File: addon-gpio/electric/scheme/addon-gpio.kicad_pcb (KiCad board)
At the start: 2 copper layers, 85 x 56 mm, 69 parts, among them K1 swd, K10 CONN_3, K11 CONN_3, K12 CONN_3, K13 CONN_3, K14 CONN_3, K15 CONN_3, K16 CONN_3, K17 CONN_3, K18 CONN_3, K19 CONN_3, K2 CONN_3, K20 CONN_3, K21 CONN_3, K22 CONN_3, K23 CONN_3, K24 CONN_3, K25 CONN_3, K26 CONN_3, K27 CONN_3, K28 CONN_3, K29 CONN_3, K3 CONN_3, K30 CONN_3, K31 CONN_3, K32 CONN_3, K4 CONN_3, K5 CONN_3, K6 CONN_3, K7 CONN_3, K8 CONN_3, K9 CONN_3, P1 TST, P2 cross board conn, P3 cross board conn, P4 TST, P5 boot-sel, P6 pwr-ext, P7 rst-2, P8 rst-1, Q1 bc847, Q2 sot223, Q3 IRLML2244, Q4 sot223, Q5 IRLML2244, X1 8MHz

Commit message: Placing components...
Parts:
- C11, C9, Q1, Q2, Q3, Q4, Q5, R10, R6, R7, R8, R9: moved to F.Cu
- moved K5 52.3 mm to (213.6, 129.0), turned to 90 degrees
- moved K6 50.5 mm to (211.1, 129.0), turned to 90 degrees
- moved K7 49.2 mm to (208.5, 129.0), turned to 90 degrees
- moved K11 49.0 mm to (198.4, 129.0), turned to 90 degrees
- moved K8 48.3 mm to (206.0, 129.0), turned to 90 degrees
- moved K10 48.2 mm to (200.9, 129.0), turned to 90 degrees
- moved K9 48.0 mm to (203.5, 129.0), turned to 90 degrees
- moved R6 27.4 mm to (216.7, 179.4)
- moved R7 23.8 mm to (216.7, 177.6)
- moved Q1 18.7 mm to (216.7, 175.0)
- moved C12 18.5 mm to (217.3, 156.6)
- moved C10 16.9 mm to (222.6, 174.1), turned to 270 degrees
- moved C9 14.9 mm to (220.4, 173.1), turned to 270 degrees
- moved K13 13.5 mm to (173.0, 129.0)
- moved K17 13.5 mm to (162.8, 129.0)
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
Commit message: Routing...
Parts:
- added K33: CONN_3, PIN_ARRAY_3X1, F.Cu at (190.8, 129.0)
- moved R3 32.3 mm to (189.6, 135.2), turned to 90 degrees
- moved K19 25.4 mm to (216.2, 129.0)
- moved P5 22.4 mm to (161.6, 148.2)
- moved R2 22.4 mm to (161.6, 145.9)
- moved K30 10.2 mm to (160.3, 129.0)
- moved K31 10.2 mm to (157.7, 129.0)
- moved K32 10.2 mm to (155.2, 129.0)
- moved K20 7.62 mm to (152.7, 129.0)
- moved K21 7.62 mm to (150.1, 129.0)
- moved K29 7.62 mm to (145.0, 129.0)
- moved K22 7.62 mm to (147.6, 129.0)
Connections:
- K10 pad 1: /pin_5 -> /pin_6
- K11 pad 1: /pin_6 -> /pin_7
- K12 pad 1: /pin_7 -> /pin_13
- K18 pad 1: /pin_13 -> /pin_14
- K19 pad 1: /pin_14 -> /pin_0
- K5 pad 1: /pin_0 -> /pin_1
- K6 pad 1: /pin_1 -> /pin_2
- K7 pad 1: /pin_2 -> /pin_3
- K8 pad 1: /pin_3 -> /pin_4
- K9 pad 1: /pin_4 -> /pin_5
- R3 pad 1: /pin_25 -> /pin_28
- stm1 pad 2: /pwr-en -> /pin_24
- stm1 pad 20: /pin_25 -> /pin_28
- stm1 pad 4: /pin_24 -> /pwr-en
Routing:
- net /pin_24: track 0.00 -> 59.1 mm
- net /pin_0: track 0.00 -> 48.0 mm
- net /pin_17: track 0.00 -> 47.4 mm
- net /pin_1: track 0.00 -> 45.4 mm
- net /pin_16: track 0.00 -> 44.5 mm
- net /pin_2: track 0.00 -> 42.8 mm
- net /pin_3: track 0.00 -> 36.0 mm
- net /pin_15: track 0.00 -> 35.9 mm
- net /pin_4: track 0.00 -> 33.9 mm
- net /pin_27: track 0.00 -> 33.8 mm
- net /pin_5: track 0.00 -> 32.2 mm
- net /pin_26: track 0.00 -> 30.9 mm
- net /pin_6: track 0.00 -> 30.5 mm
- net /pin_12: track 0.00 -> 29.7 mm
- net /pin_25: track 0.00 -> 28.8 mm
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
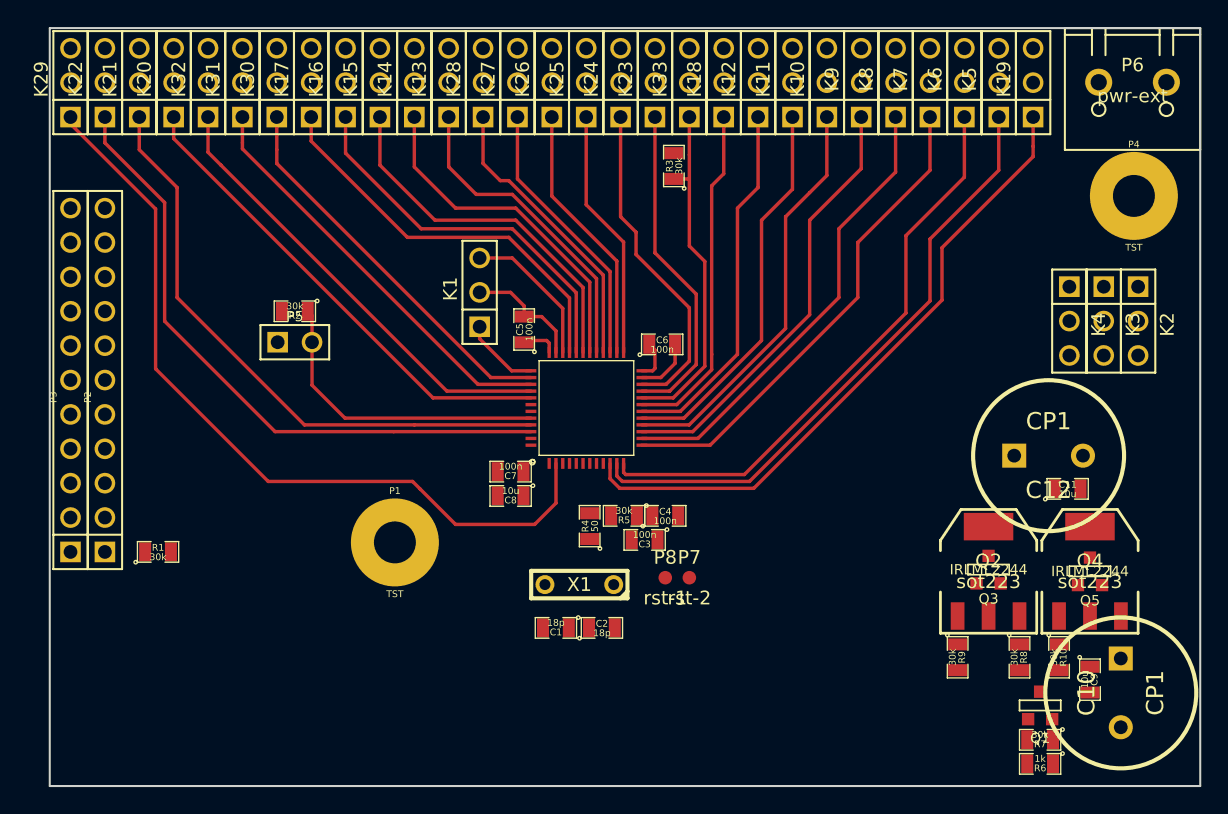
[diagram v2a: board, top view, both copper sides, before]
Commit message: Routed. Making silcography.
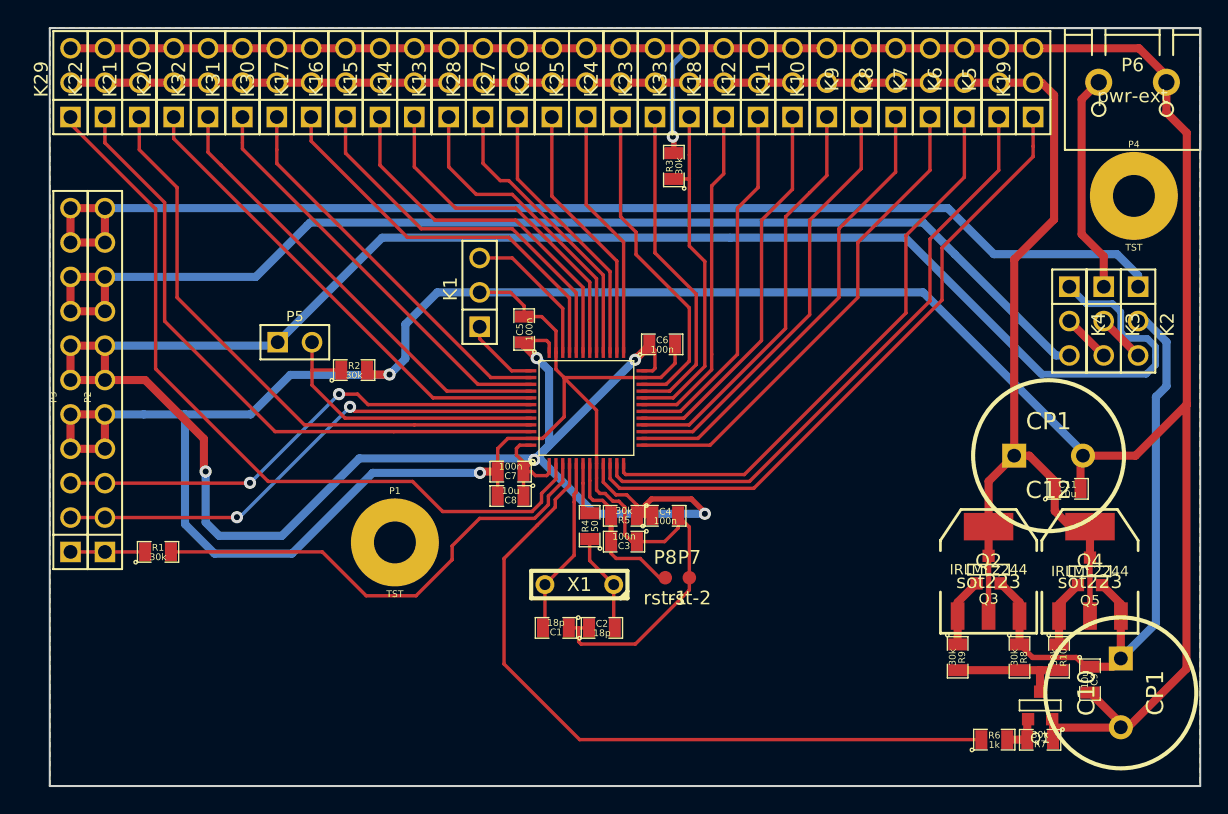
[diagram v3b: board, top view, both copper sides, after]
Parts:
- moved R2 6.17 mm to (166.0, 150.3), turned to 0 degrees
- moved R6 3.83 mm to (213.3, 177.6), turned to 0 degrees
- moved C3 1.53 mm to (185.9, 162.9)
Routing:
- net GND: track 13.2 -> 363.2 mm, vias 0 -> 3
- net VDD: track 5.68 -> 211.6 mm, vias 0 -> 5
- net /pwr-servo: track 0.00 -> 129.2 mm
- net /batt+: track 0.00 -> 89.4 mm
- net /+5v: track 0.00 -> 87.1 mm
- net /pwr-en: track 0.00 -> 54.4 mm
- net N-0000020: track 0.00 -> 47.0 mm
- net /sda-int: track 0.00 -> 37.5 mm, vias 0 -> 2
- net /scl-int: track 0.38 -> 37.1 mm, vias 0 -> 2
- net /wakeup: track 0.00 -> 36.1 mm
- net /pwr-ext: track 0.00 -> 16.3 mm
- net N-0000018: track 0.00 -> 13.2 mm
- net N-0000011: track 0.00 -> 12.5 mm
- net N-0000019: track 0.00 -> 9.08 mm
- net N-0000017: track 0.00 -> 7.34 mm
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- added copper zone on B.Cu, net GND
- added copper zone on F.Cu, net GND
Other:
- board text added: "3.3"
- board text added: "batt"
- board text added: "ext"

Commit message: Made drawing with connections scheme.
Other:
- board text added: "5v"
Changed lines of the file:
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@@
     (area 127.606667 112.000001 242.964763 190.8)
     (thickness 1.6)
-    (drawings 53)
+    (drawings 69)
     (tracks 551)
     (zones 0)
@@
   )
   (setup
-    (last_trace_width 0.4)
+    (last_trace_width 0.254)
     (user_trace_width 0.4)
     (user_trace_width 0.5)
@@
     )
   )
+  (gr_line (start 211 154) (end 211 151) (angle 90) (layer Eco1.User) (width 0.2))
+  (gr_line (start 214.5 154) (end 214.5 151) (angle 90) (layer Eco1.User) (width 0.2))
+  (gr_line (start 213 152.5) (end 214.5 154) (angle 90) (layer Eco1.User) (width 0.2))
+  (gr_line (start 214.5 151) (end 213 152.5) (angle 90) (layer Eco1.User) (width 0.2))
+  (gr_line (start 209.5 152.5) (end 211 154) (angle 90) (layer Eco1.User) (width 0.2))
+  (gr_line (start 211 151) (end 209.5 152.5) (angle 90) (layer Eco1.User) (width 0.2))
+  (gr_text 5v (at 206.75 152.25 90) (layer Eco1.User)
+    (effects (font (size 2 2) (thickness 0.3)))
+  )
+  (gr_line (start 212 149.75) (end 212 141.75) (angle 90) (layer Eco1.User) (width 0.2))
+  (gr_line (start 208.5 149.75) (end 208.5 141.75) (angle 90) (layer Eco1.User) (width 0.2))
+  (gr_line (start 205.25 149.75) (end 205.25 141.75) (angle 90) (layer Eco1.User) (width 0.2))
+  (gr_line (start 215 149.75) (end 205.25 149.75) (angle 90) (layer Eco1.User) (width 0.2))
+  (gr_line (start 215 141.75) (end 215 149.75) (angle 90) (layer Eco1.User) (width 0.2))
+  (gr_line (start 205.25 141.75) (end 215 141.75) (angle 90) (layer Eco1.User) (width 0.2))
+  (gr_circle (center 213.75 148.5) (end 214.5 148.75) (layer Eco1.User) (width 0.2))
+  (gr_circle (center 210.25 148.5) (end 211 148.5) (layer Eco1.User) (width 0.2))
+  (gr_circle (center 206.5 148.5) (end 207.25 148.75) (layer Eco1.User) (width 0.2))
   (gr_circle (center 213.75 145.75) (end 213.75 145) (layer Eco1.User) (width 0.2))
   (gr_circle (center 210.25 145.75) (end 210.25 145) (layer Eco1.User) (width 0.2))
